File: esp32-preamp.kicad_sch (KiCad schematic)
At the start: 40 parts, among them J1 PWR IN, J10 TSOP382, J2 OUT, J3 LFE, J4 INPUT 1, J5 INPUT 2, J6 INPUT 2, J7 AMP PWR, J8 POT MOTOR, J9 VOLUME, Q1 2N3904, Q2 2N3904, Q3 2N3904, Q4 2N3904, U1 ESP32 D1 Mini, U2 TSR0.5-2450

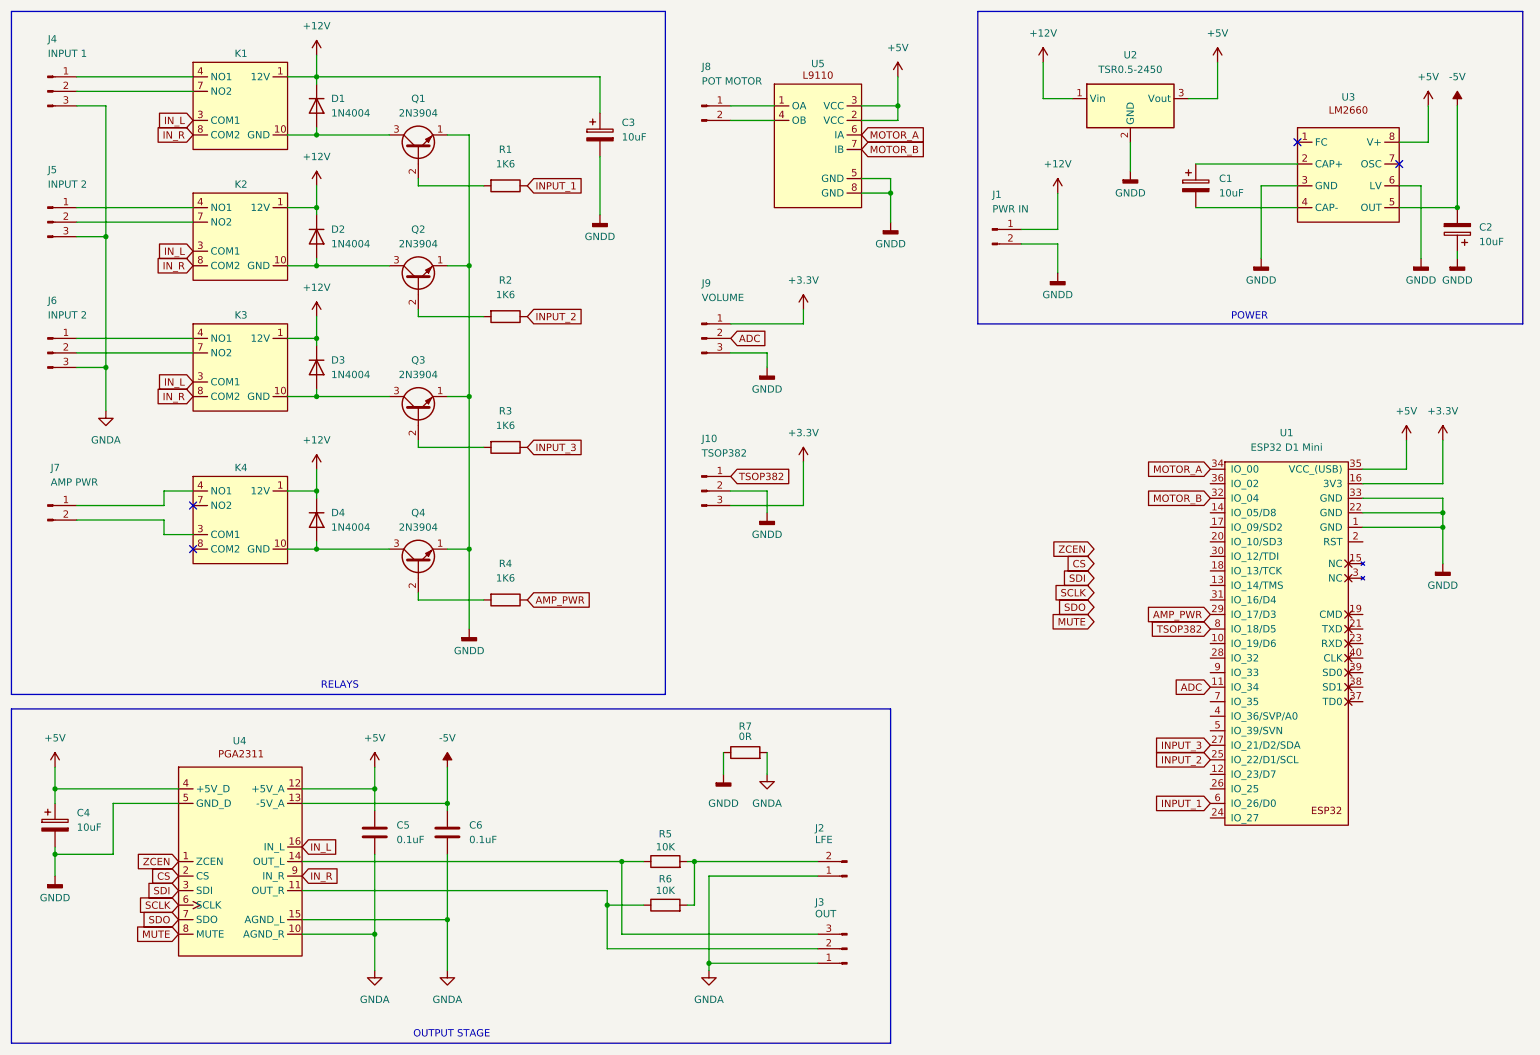
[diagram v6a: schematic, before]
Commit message: Add more decoupling caps
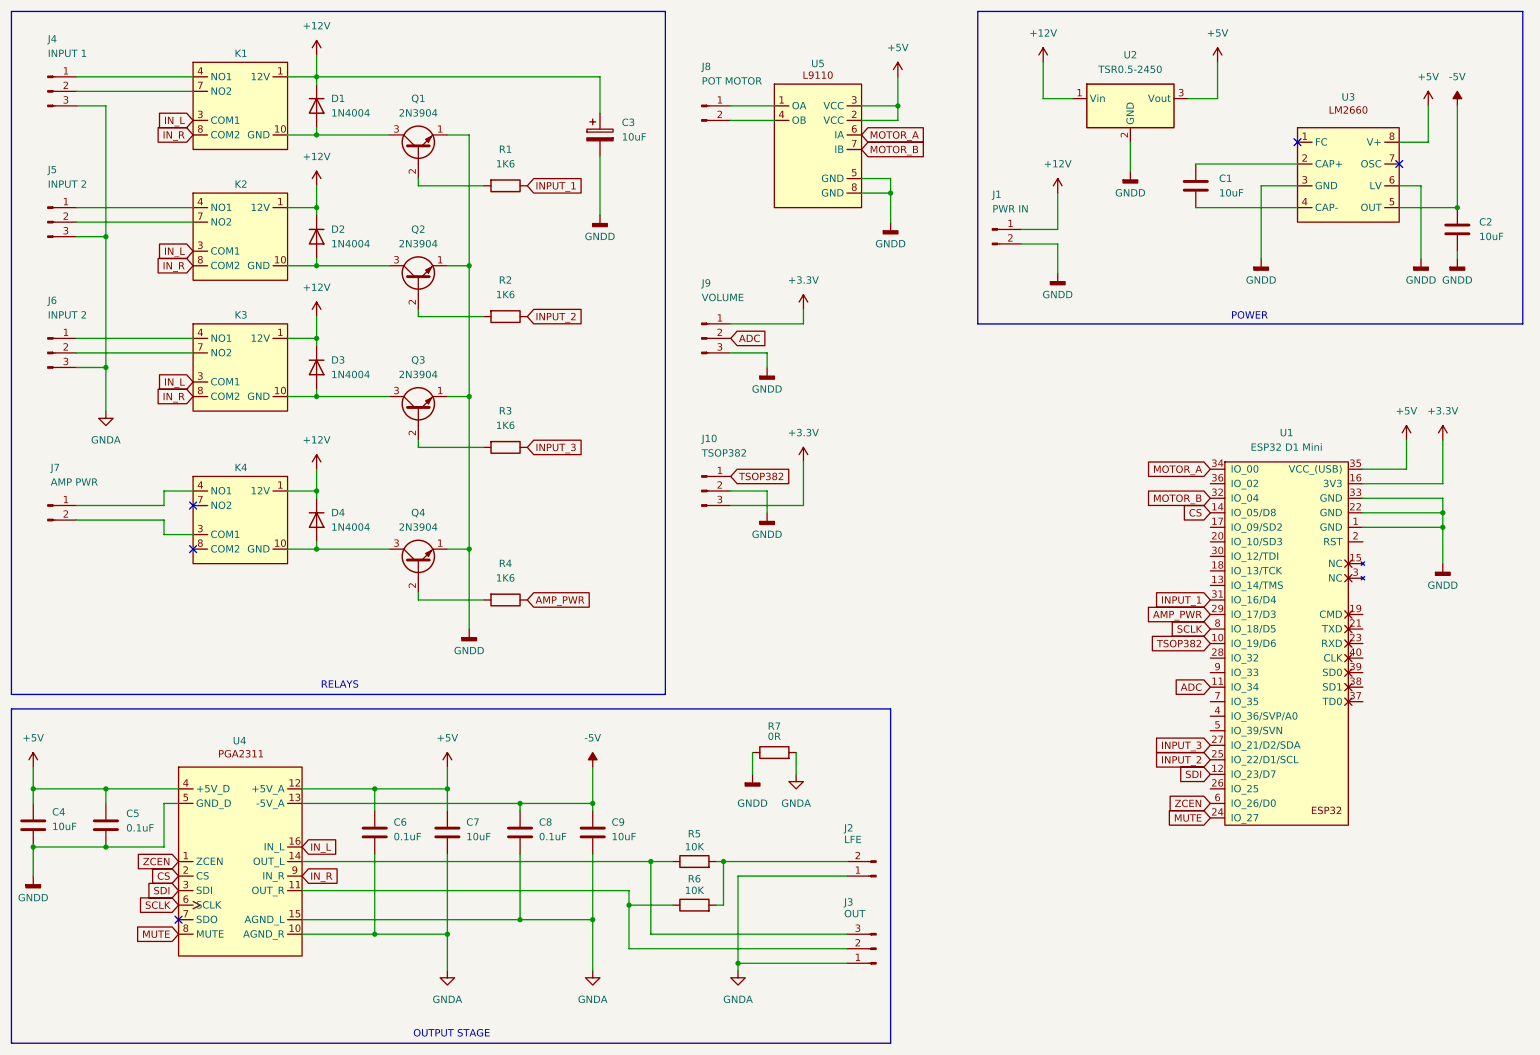
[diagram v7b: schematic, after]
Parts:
- added C5, C6, C8: 0.1uF, symbol Device:C
- C1, C2, C4: symbol Device:C_Polarized -> Device:C
- C7: renamed from C5; value 0.1uF -> 10uF
- C9: renamed from C6; value 0.1uF -> 10uF
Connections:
- net +5V: now also C5.1, C6.1
- net -5V: now also C8.1
- net CS: now also U1.14 (IO_05/D8)
- net GNDA: now also C6.2, C8.2
- net GNDD: now also C5.2
- net INPUT_1: now also U1.31 (IO_16/D4); no longer U1.6 (IO_26/D0)
- net MUTE: now also U1.24 (IO_27)
- net SCLK: now also U1.8 (IO_18/D5)
- net SDI: now also U1.12 (IO_23/D7)
- net TSOP382: now also U1.10 (IO_19/D6); no longer U1.8 (IO_18/D5)
- net ZCEN: now also U1.6 (IO_26/D0)
- net SDO: no longer names the net of U4.7 (SDO)
- no-connect marks 4 -> 5
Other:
- moved on the sheet: C7, C9, J2, J3, R5, R6, R7

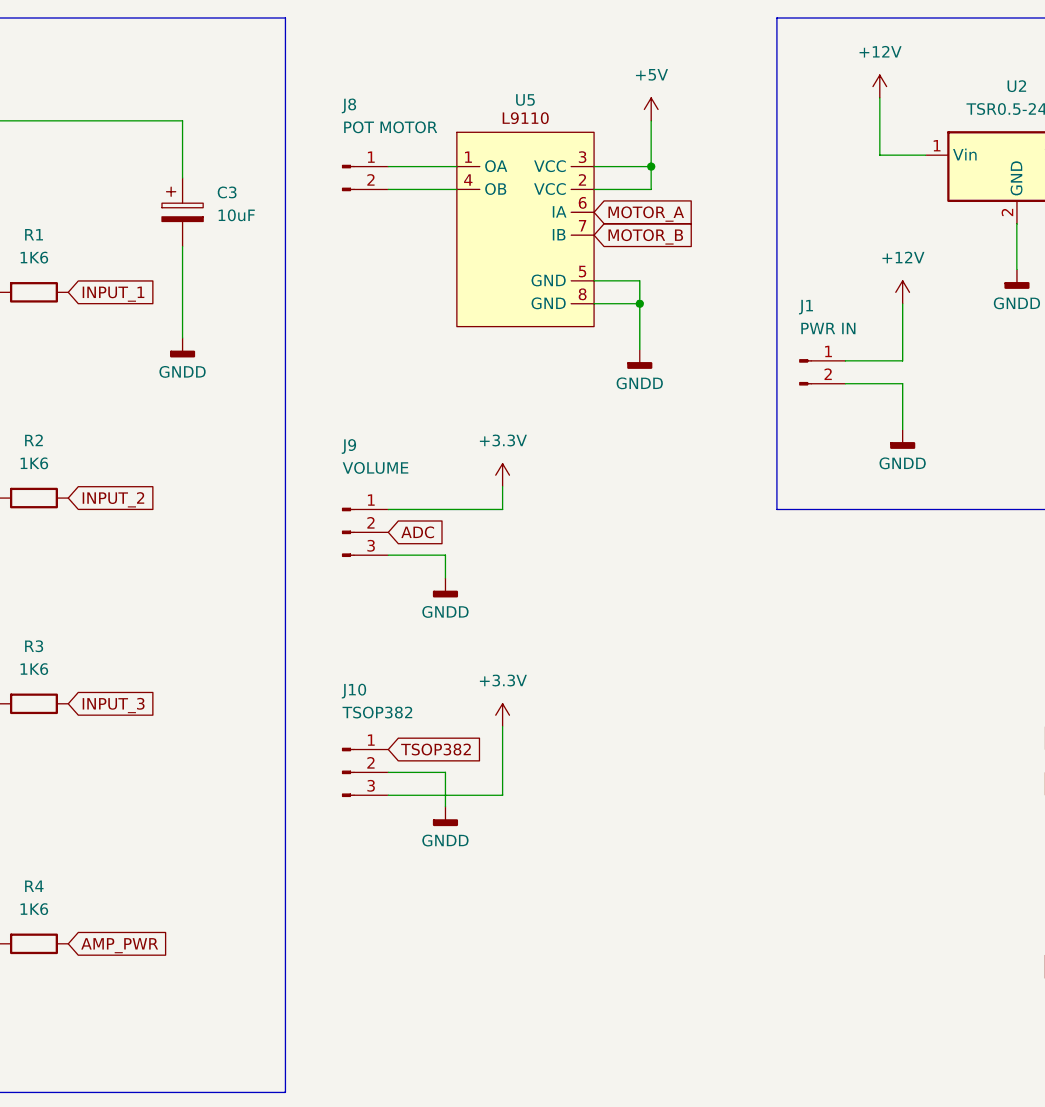
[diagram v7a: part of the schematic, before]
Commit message: Add 120uF cap to motor driver
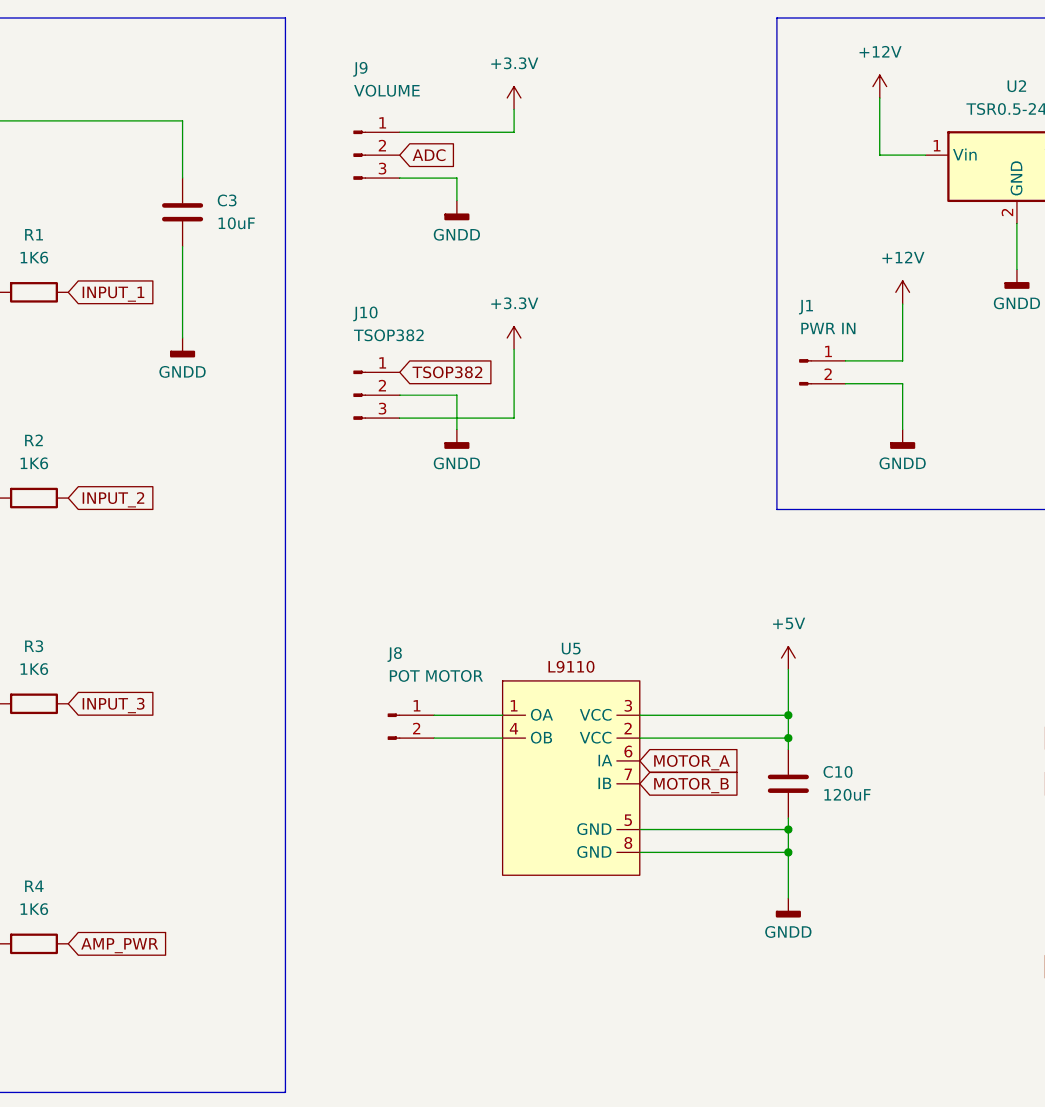
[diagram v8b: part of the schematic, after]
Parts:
- added C10: 120uF, symbol Device:C
- C3: symbol Device:C_Polarized -> Device:C
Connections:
- net +5V: now also C10.1
- net GNDD: now also C10.2
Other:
- moved on the sheet: J10, J8, J9, U5
